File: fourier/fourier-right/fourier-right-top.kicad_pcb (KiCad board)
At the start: 2 copper layers, 141.4 x 92.2 mm, 7 parts

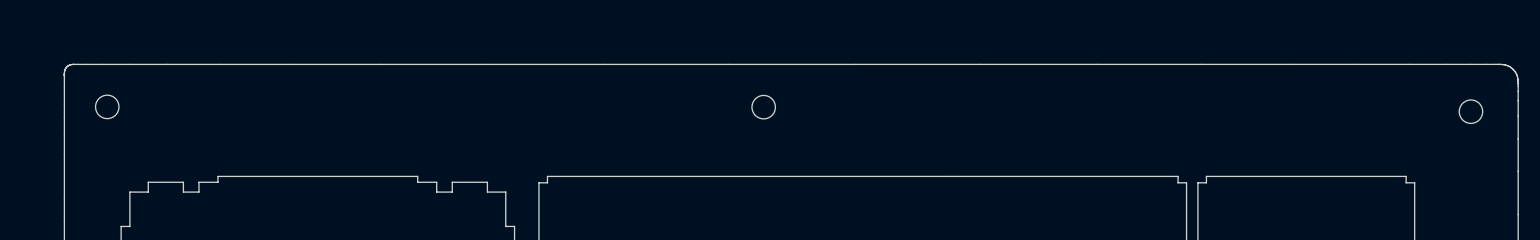
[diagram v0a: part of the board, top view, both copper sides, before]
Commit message: Top height and center hole adjusment
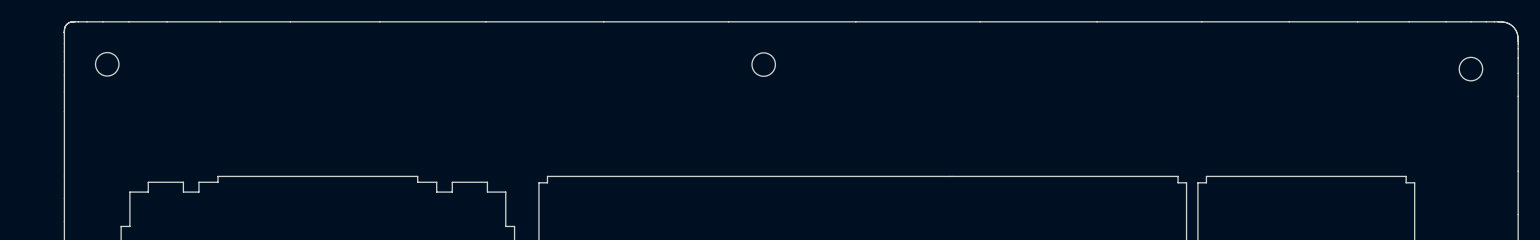
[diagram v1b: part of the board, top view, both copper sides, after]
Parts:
- moved REF** 4.00 mm to (28.4, 22.1)
- moved REF** 4.00 mm to (90.0, 22.1)
- moved REF** 4.00 mm to (156.5, 22.6)
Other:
- board size 141.4 x 92.2 mm -> 141.4 x 96.2 mm

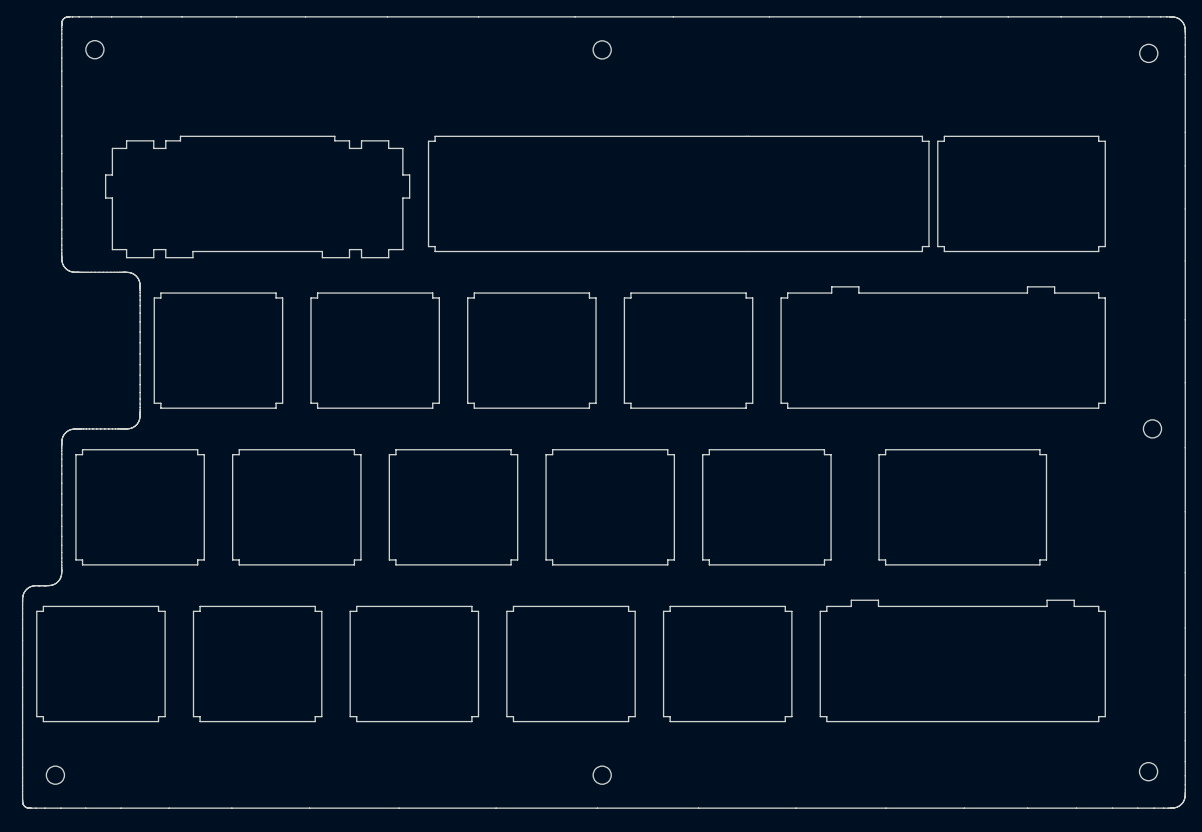
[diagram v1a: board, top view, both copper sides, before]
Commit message: rotate right top to correct orientation and upgraded to KiCad 5.99
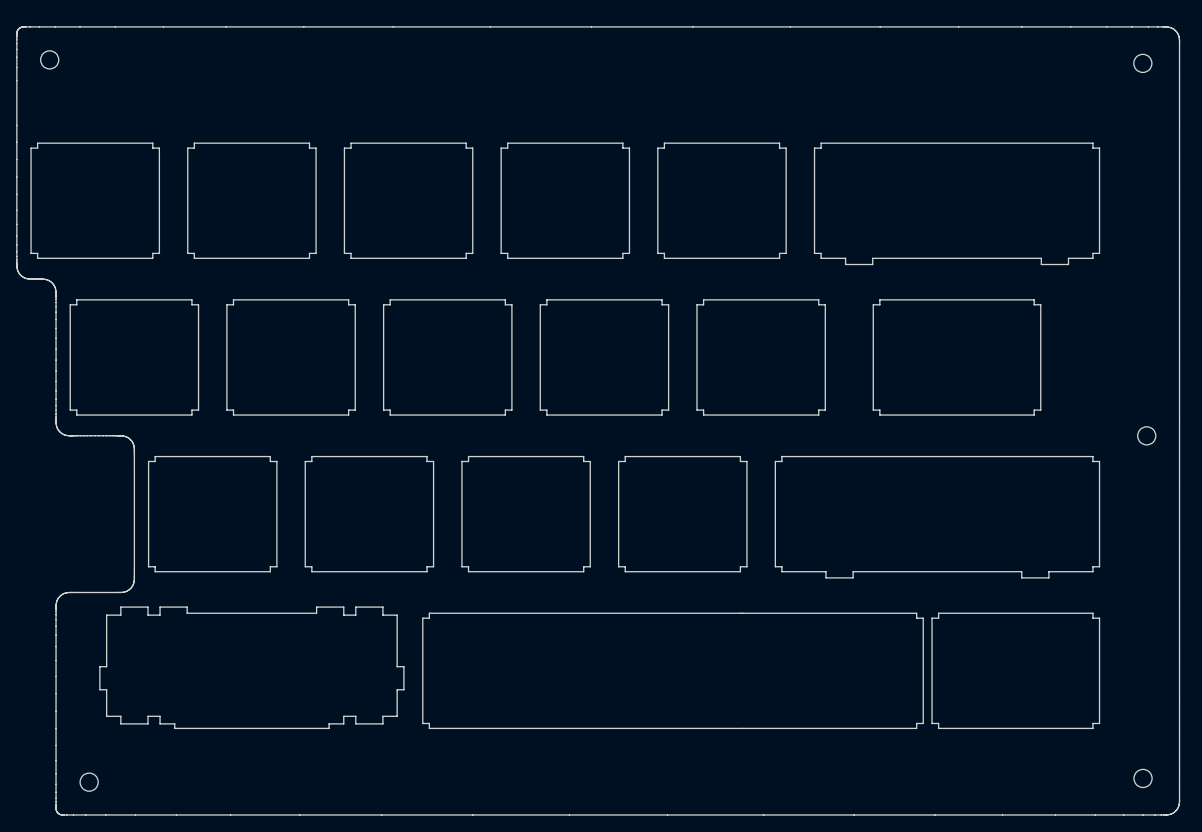
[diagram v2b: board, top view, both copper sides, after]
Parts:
- removed the REF** at (28.4, 22.1)
- removed the REF** at (90.0, 22.1)
- removed the REF** at (156.5, 22.6)
- removed the REF** at (156.9, 68.2)
- removed the REF** at (156.4, 109.9)
- removed the REF** at (90.0, 110.3)
- removed the REF** at (23.6, 110.3)
- added REF**: MountingHole_2.2mm_M2, Mounting_Holes:MountingHole_2.2mm_M2, B.Cu at (155.8, 23.8)
- added REF**: MountingHole_2.2mm_M2, Mounting_Holes:MountingHole_2.2mm_M2, B.Cu at (156.2, 69.0)
- added REF**: MountingHole_2.2mm_M2, Mounting_Holes:MountingHole_2.2mm_M2, B.Cu at (155.8, 110.7)
- added REF**: MountingHole_2.2mm_M2, Mounting_Holes:MountingHole_2.2mm_M2, B.Cu at (27.7, 111.1)
- added REF**: MountingHole_2.2mm_M2, Mounting_Holes:MountingHole_2.2mm_M2, B.Cu at (22.9, 23.3)
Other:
- board size 141.4 x 96.2 mm -> 141.4 x 95.8 mm
- net class Default removed
